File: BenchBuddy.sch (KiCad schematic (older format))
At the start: 0 parts

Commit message: Understanding the LED Driver Module
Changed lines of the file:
@@
 F0 "LED_Driver" 50
 F1 "LED_Driver.sch" 50
-F2 "EN" I L 6750 3250 60
-F3 "FREQ" I L 6750 3450 60
-F4 "String+" O R 8900 3250 60
-F5 "String-" I R 8900 3450 60
+F2 "String+" O R 8900 3250 60
+F3 "String-" I R 8900 3450 60
+F4 "LED_EN_PWM" I L 6750 3300 60
 $EndSheet
 $Sheet

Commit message: Understanding the Arduino Module
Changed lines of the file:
@@
 LIBS:valves
 LIBS:MyComponents
+LIBS:arduino_shieldsNCL
 LIBS:BenchBuddy-cache
 EELAYER 24 0
@@
 F2 "Relay+" O R 3450 6650 60
 F3 "Relay-" I R 3450 6850 60
-F4 "MOSI" O R 3450 5900 60
-F5 "MISO" I R 3450 6000 60
+F4 "MOSI" O R 3450 6050 60
+F5 "MISO" I R 3450 5950 60
 F6 "SCLK" O R 3450 6150 60
-F7 "CS_N" O R 3450 6300 60
-F8 "LED_EN" O R 3450 5300 60
-F9 "LED_FREQ" O R 3450 5450 60
-F10 "FAN_EN" O R 3450 4750 60
-F11 "FAN_MEAS" I R 3450 4950 60
+F7 "FAN_EN_N" O R 3450 5250 60
+F8 "CURR_MEAS" I R 3450 5450 60
+F9 "LED_EN_PWM" O R 3450 4750 60
+F10 "TACH_MEAS" I R 3450 5600 60
+F11 "V+_ADJ_MON" I R 3450 4000 60
+F12 "V-_ADJ_MON" I R 3450 4150 60
+F13 "DAC_CS_N" O R 3450 6250 60
+F14 "ADC_CS_N" O R 3450 6350 60
 $EndSheet
 $Sheet
@@
 F0 "Thermocouple" 50
 F1 "Thermocouple.sch" 50
-F2 "MOSI" I L 6750 4150 60
-F3 "MISO" O L 6750 4300 60
+F2 "MOSI" I L 6750 4350 60
+F3 "MISO" O L 6750 4250 60
 F4 "SCLK" I L 6750 4450 60
-F5 "CS_N" I L 6750 4600 60
+F5 "CS_N" I L 6750 4550 60
 F6 "TC_IN+" I R 8900 4200 60
 F7 "TC_IN-" I R 8900 4400 60
@@
 $EndSheet
 $Sheet
-S 6750 3050 2150 550
-U 52EA35F8
-F0 "LED_Driver" 50
-F1 "LED_Driver.sch" 50
-F2 "String+" O R 8900 3250 60
-F3 "String-" I R 8900 3450 60
-F4 "LED_EN_PWM" I L 6750 3300 60
-$EndSheet
-$Sheet
 S 9400 800  1450 5300
 U 52EA3891
 F0 "Terminal_Block" 50
 F1 "Terminal_Block.sch" 50
-$EndSheet
-$Sheet
-S 6750 1650 2150 1100
-U 52EA3640
-F0 "Fan" 50
-F1 "Fan.sch" 50
-F2 "Power+" O R 8900 1850 60
-F3 "Power-" I R 8900 2000 60
-F4 "Tach_In" I R 8900 2150 60
-F5 "Tach_Out" O L 6750 2600 60
-F6 "Fan_In" I L 6750 1750 60
-F7 "MISO" O L 6750 1950 60
-F8 "MOSI" I L 6750 2050 60
-F9 "SCLK" I L 6750 2150 60
-F10 "CS_N" I L 6750 2250 60
-F11 "Current_Measure" O L 6750 2450 60
+F2 "V+_ADJ" O L 9400 1150 60
+F3 "V-_ADJ" O L 9400 1350 60
+F4 "FAN_OUT+" O L 9400 2850 60
+F5 "FAN_OUT-" O L 9400 3000 60
+F6 "TACH_IN" I L 9400 3600 60
+F7 "LED_STRING+" O L 9400 2050 60
+F8 "LED_STRING-" O L 9400 2200 60
+F9 "RELAY_NC" B L 9400 5700 60
+F10 "RELAY_NO" B L 9400 5550 60
+F11 "RELAY_COM" B L 9400 5400 60
+F12 "TC_IN+" I L 9400 4200 60
+F13 "TC_IN-" I L 9400 4400 60
 $EndSheet
 $Sheet
@@
 F0 "Relay" 50
 F1 "Relay.sch" 50
-F2 "DIN+" I L 6750 5350 60
-F3 "DIN-" O L 6750 5700 60
-F4 "NC" B R 8900 5400 60
-F5 "NO" B R 8900 5700 60
-F6 "COM" B R 8900 5550 60
-$EndSheet
+F2 "RELAY_NC" B R 8900 5700 60
+F3 "RELAY_NO" B R 8900 5550 60
+F4 "RELAY_COM" B R 8900 5400 60
+F5 "RELAY+" I L 6750 5400 60
+F6 "RELAY-" O L 6750 5550 60
+$EndSheet
+$Sheet
+S 6750 1850 2150 550
+U 52EA35F8
+F0 "LED_Driver" 50
+F1 "LED_Driver.sch" 50
+F2 "LED_EN_PWM" I L 6750 2250 60
+F3 "LED_STRING+" O R 8900 2050 60
+F4 "LED_STRING-" O R 8900 2200 60
+$EndSheet
+Wire Wire Line
+	9400 1150 6300 1150
+Wire Wire Line
+	9400 1350 6300 1350
+Wire Wire Line
+	9400 5400 8900 5400
+Wire Wire Line
+	8900 5550 9400 5550
+Wire Wire Line
+	9400 5700 8900 5700
+Wire Wire Line
+	8900 4200 9400 4200
+Wire Wire Line
+	8900 4400 9400 4400
+Wire Wire Line
+	3450 4000 3800 4000
+Wire Wire Line
+	3800 4000 3800 1450
+Wire Wire Line
+	3800 1450 4150 1450
+Wire Wire Line
+	3450 4150 4000 4150
+Wire Wire Line
+	4000 4150 4000 1550
+Wire Wire Line
+	4000 1550 4150 1550
+$Sheet
+S 6750 2650 2150 1100
+U 52EA3640
+F0 "Fan" 50
+F1 "Fan.sch" 50
+F2 "MISO" O L 6750 3250 60
+F3 "MOSI" I L 6750 3350 60
+F4 "SCLK" I L 6750 3450 60
+F5 "CS_N" I L 6750 3550 60
+F6 "FAN_OUT+" O R 8900 2850 60
+F7 "TACH_IN" I R 8900 3600 60
+F8 "TACH_MEAS" O L 6750 3050 60
+F9 "FAN_EN_N" I L 6750 2800 60
+F10 "CURR_MEAS" O L 6750 2900 60
+F11 "FAN_OUT-" O R 8900 3000 60
+$EndSheet
+Wire Wire Line
+	9400 2050 8900 2050
+Wire Wire Line
+	8900 2200 9400 2200
+Wire Wire Line
+	9400 2850 8900 2850
+Wire Wire Line
+	8900 3000 9400 3000
+Wire Wire Line
+	9400 3600 8900 3600
+Wire Wire Line
+	6750 2250 4650 2250
+Wire Wire Line
+	4650 2250 4650 4750
+Wire Wire Line
+	4650 4750 3450 4750
+Wire Wire Line
+	3450 5250 5150 5250
+Wire Wire Line
+	5150 5250 5150 2800
+Wire Wire Line
+	5150 2800 6750 2800
+Wire Wire Line
+	3450 5450 5300 5450
+Wire Wire Line
+	5300 5450 5300 2900
+Wire Wire Line
+	5300 2900 6750 2900
+Wire Wire Line
+	3450 5600 5400 5600
+Wire Wire Line
+	5400 5600 5400 3050
+Wire Wire Line
+	5400 3050 6750 3050
+Wire Wire Line
+	3450 5950 5600 5950
+Wire Wire Line
+	5600 5950 5600 4250
+Wire Wire Line
+	5600 4250 5600 3250
+Wire Wire Line
+	5600 3250 6750 3250
+Wire Wire Line
+	6750 3350 5700 3350
+Wire Wire Line
+	5700 3350 5700 4350
+Wire Wire Line
+	5700 4350 5700 6050
+Wire Wire Line
+	5700 6050 3450 6050
+Wire Wire Line
+	3450 6150 5800 6150
+Wire Wire Line
+	5800 6150 5800 4450
+Wire Wire Line
+	5800 4450 5800 3450
+Wire Wire Line
+	5800 3450 6750 3450
+Wire Wire Line
+	6750 5400 6200 5400
+Wire Wire Line
+	6200 5400 6200 6650
+Wire Wire Line
+	6200 6650 3450 6650
+Wire Wire Line
+	3450 6850 6350 6850
+Wire Wire Line
+	6350 6850 6350 5550
+Wire Wire Line
+	6350 5550 6750 5550
+Wire Wire Line
+	3450 6250 5900 6250
+Wire Wire Line
+	5900 6250 5900 3550
+Wire Wire Line
+	5900 3550 6750 3550
+Wire Wire Line
+	6750 4250 5600 4250
+Connection ~ 5600 4250
+Wire Wire Line
+	6750 4350 5700 4350
+Connection ~ 5700 4350
+Wire Wire Line
+	6750 4450 5800 4450
+Connection ~ 5800 4450
+Wire Wire Line
+	6750 4550 6000 4550
+Wire Wire Line
+	6000 4550 6000 6350
+Wire Wire Line
+	6000 6350 3450 6350
 $EndSCHEMATC

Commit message: Revisting the Current/Fan Module
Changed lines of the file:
@@
 F5 "MISO" I R 3450 5950 60
 F6 "SCLK" O R 3450 6150 60
-F7 "FAN_EN_N" O R 3450 5250 60
-F8 "CURR_MEAS" I R 3450 5450 60
-F9 "LED_EN_PWM" O R 3450 4750 60
-F10 "TACH_MEAS" I R 3450 5600 60
-F11 "V+_ADJ_MON" I R 3450 4000 60
-F12 "V-_ADJ_MON" I R 3450 4150 60
-F13 "DAC_CS_N" O R 3450 6250 60
-F14 "ADC_CS_N" O R 3450 6350 60
+F7 "CURR_MEAS" I R 3450 5500 60
+F8 "LED_EN_PWM" O R 3450 4750 60
+F9 "TACH_MEAS" I R 3450 5600 60
+F10 "V+_ADJ_MON" I R 3450 4000 60
+F11 "V-_ADJ_MON" I R 3450 4150 60
+F12 "DAC_CS_N" O R 3450 6250 60
+F13 "ADC_CS_N" O R 3450 6350 60
+F14 "FAN_PWM" O R 3450 5250 60
+F15 "FAN_MODE" O R 3450 5350 60
 $EndSheet
 $Sheet
@@
 F0 "Fan" 50
 F1 "Fan.sch" 50
-F2 "MISO" O L 6750 3250 60
-F3 "MOSI" I L 6750 3350 60
-F4 "SCLK" I L 6750 3450 60
-F5 "CS_N" I L 6750 3550 60
+F2 "MISO" O L 6750 3350 60
+F3 "MOSI" I L 6750 3450 60
+F4 "SCLK" I L 6750 3550 60
+F5 "CS_N" I L 6750 3650 60
 F6 "FAN_OUT+" O R 8900 2850 60
 F7 "TACH_IN" I R 8900 3600 60
-F8 "TACH_MEAS" O L 6750 3050 60
-F9 "FAN_EN_N" I L 6750 2800 60
-F10 "CURR_MEAS" O L 6750 2900 60
-F11 "FAN_OUT-" O R 8900 3000 60
+F8 "TACH_MEAS" O L 6750 3150 60
+F9 "CURR_MEAS" O L 6750 3050 60
+F10 "FAN_OUT-" O R 8900 3000 60
+F11 "FAN_PWM" I L 6750 2800 60
+F12 "FAN_MODE" O L 6750 2900 60
 $EndSheet
 Wire Wire Line
@@
 	4650 4750 3450 4750
 Wire Wire Line
-	3450 5250 5150 5250
-Wire Wire Line
-	5150 5250 5150 2800
-Wire Wire Line
-	5150 2800 6750 2800
-Wire Wire Line
-	3450 5450 5300 5450
-Wire Wire Line
-	5300 5450 5300 2900
-Wire Wire Line
-	5300 2900 6750 2900
+	3450 5250 5100 5250
+Wire Wire Line
+	5100 5250 5100 2800
+Wire Wire Line
+	5100 2800 6750 2800
+Wire Wire Line
+	3450 5500 5300 5500
+Wire Wire Line
+	5300 5500 5300 3050
+Wire Wire Line
+	5300 3050 6750 3050
 Wire Wire Line
 	3450 5600 5400 5600
 Wire Wire Line
-	5400 5600 5400 3050
-Wire Wire Line
-	5400 3050 6750 3050
-Wire Wire Line
-	3450 5950 5600 5950
-Wire Wire Line
-	5600 5950 5600 4250
-Wire Wire Line
-	5600 4250 5600 3250
-Wire Wire Line
-	5600 3250 6750 3250
-Wire Wire Line
-	6750 3350 5700 3350
-Wire Wire Line
-	5700 3350 5700 4350
+	5400 5600 5400 3150
+Wire Wire Line
+	5400 3150 6750 3150
+Wire Wire Line
+	5600 5950 3450 5950
+Wire Wire Line
+	5600 3350 5600 4250
+Wire Wire Line
+	5600 4250 5600 5950
+Wire Wire Line
+	5600 3350 6750 3350
+Wire Wire Line
+	6750 3450 5700 3450
+Wire Wire Line
+	5700 3450 5700 4350
 Wire Wire Line
 	5700 4350 5700 6050
@@
 	5700 6050 3450 6050
 Wire Wire Line
-	3450 6150 5800 6150
-Wire Wire Line
-	5800 6150 5800 4450
-Wire Wire Line
-	5800 4450 5800 3450
-Wire Wire Line
-	5800 3450 6750 3450
+	5800 6150 3450 6150
+Wire Wire Line
+	5800 3550 5800 4450
+Wire Wire Line
+	5800 4450 5800 6150
+Wire Wire Line
+	5800 3550 6750 3550
 Wire Wire Line
 	6750 5400 6200 5400
@@
 	3450 6250 5900 6250
 Wire Wire Line
-	5900 6250 5900 3550
-Wire Wire Line
-	5900 3550 6750 3550
+	5900 6250 5900 3650
+Wire Wire Line
+	5900 3650 6750 3650
 Wire Wire Line
 	6750 4250 5600 4250
@@
 Wire Wire Line
 	6000 6350 3450 6350
+Wire Wire Line
+	6750 2900 5200 2900
+Wire Wire Line
+	5200 5350 5200 2900
+Wire Wire Line
+	3450 5350 5200 5350
 $EndSCHEMATC

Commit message: Associating and Placing the Relay Module
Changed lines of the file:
@@
 	5600 5950 3450 5950
 Wire Wire Line
-	5600 3350 5600 4250
-Wire Wire Line
-	5600 4250 5600 5950
+	5600 3350 5600 5950
 Wire Wire Line
 	5600 3350 6750 3350
@@
 	6750 3450 5700 3450
 Wire Wire Line
-	5700 3450 5700 4350
-Wire Wire Line
-	5700 4350 5700 6050
+	5700 3450 5700 6050
 Wire Wire Line
 	5700 6050 3450 6050
@@
 	5800 6150 3450 6150
 Wire Wire Line
-	5800 3550 5800 4450
-Wire Wire Line
-	5800 4450 5800 6150
+	5800 3550 5800 6150
 Wire Wire Line
 	5800 3550 6750 3550
@@
 	6750 2900 5200 2900
 Wire Wire Line
-	5200 5350 5200 2900
+	5200 2900 5200 5350
 Wire Wire Line
-	3450 5350 5200 5350
+	5200 5350 3450 5350
 $EndSCHEMATC

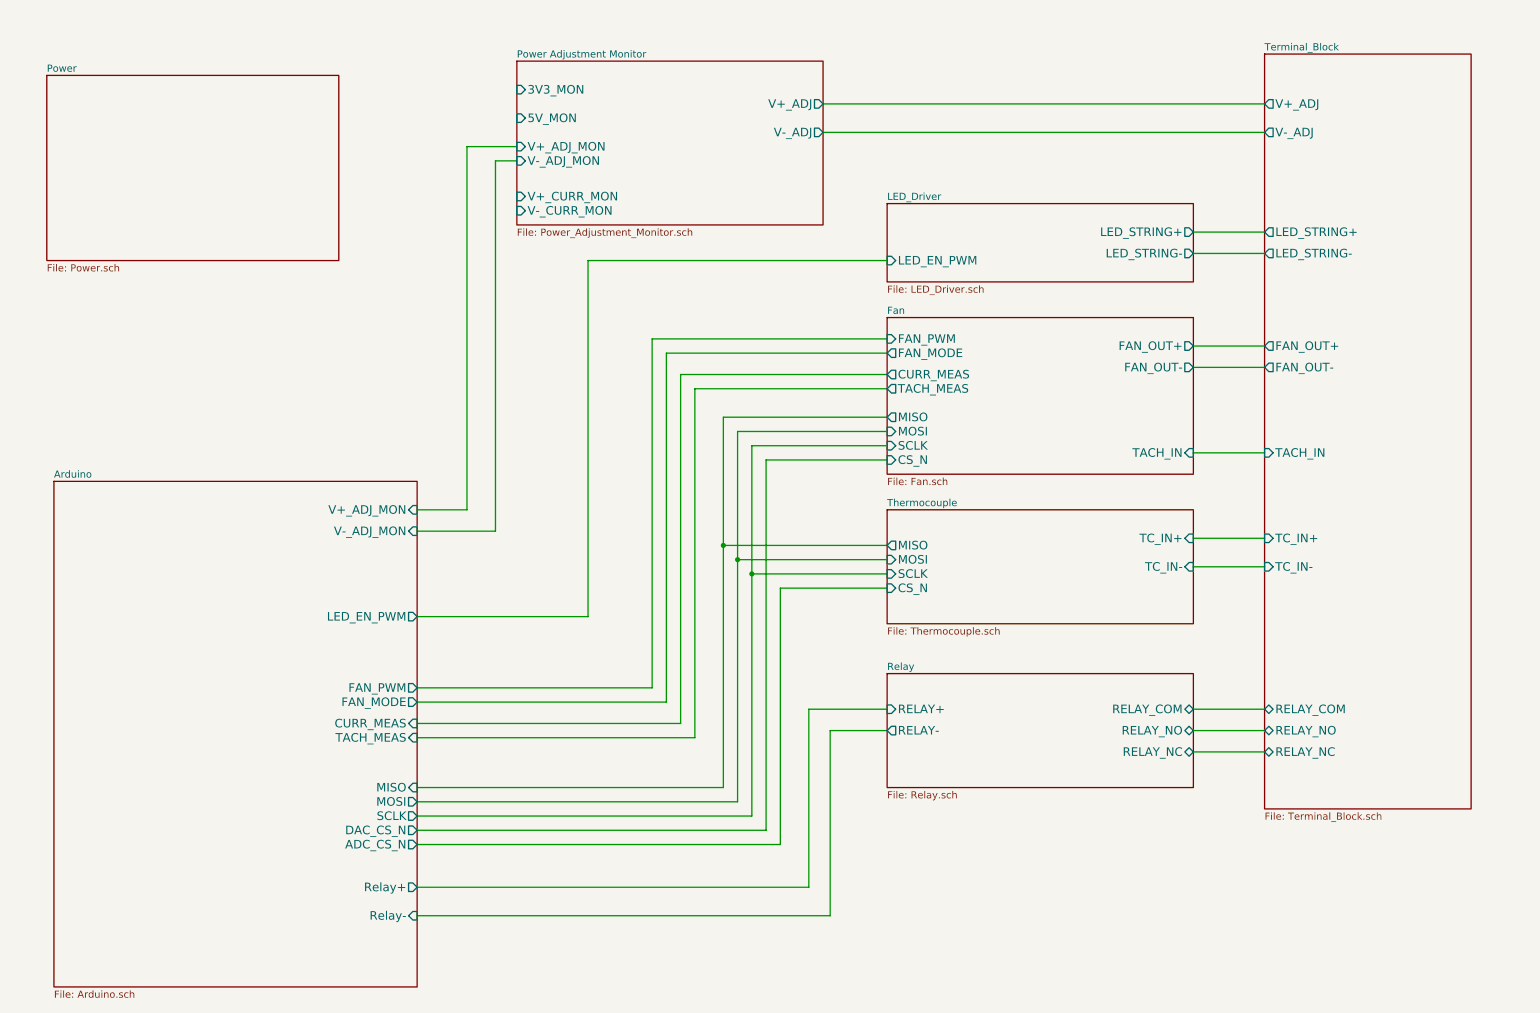
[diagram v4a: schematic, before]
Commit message: Associating and Placing the Thermocouple Module
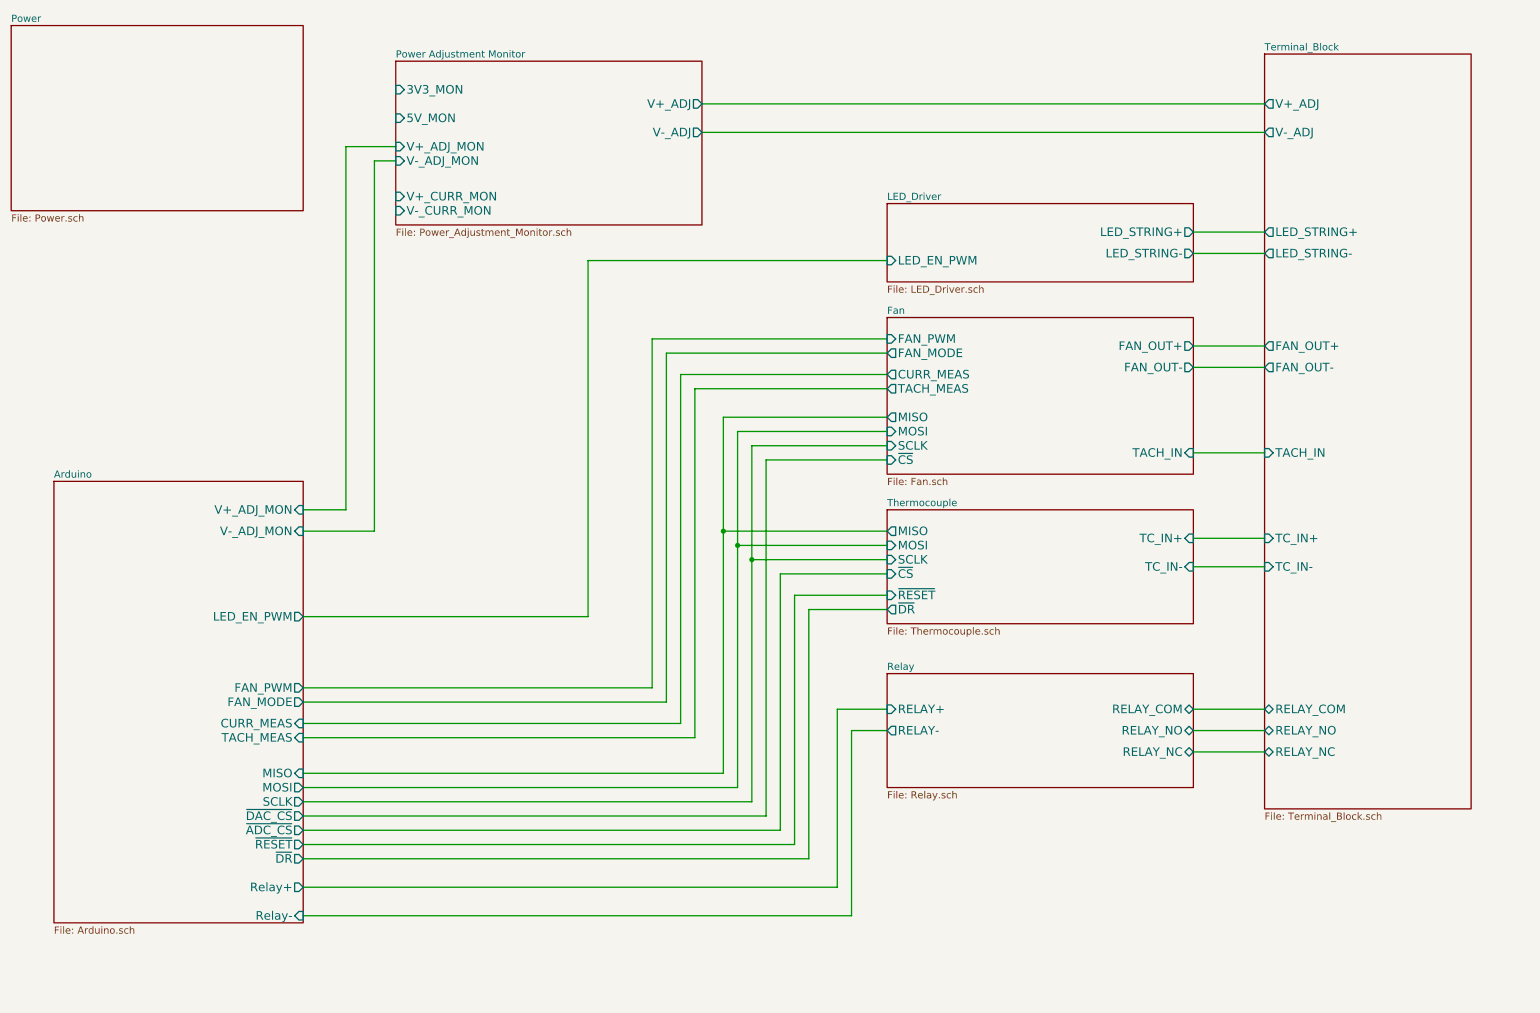
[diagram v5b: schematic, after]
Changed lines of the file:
@@
 LIBS:MyComponents
 LIBS:arduino_shieldsNCL
+LIBS:BenchBudEE
 LIBS:BenchBuddy-cache
 EELAYER 24 0
@@
 $EndDescr
 $Sheet
-S 900  3800 2550 3550
+S 900  3800 1750 3100
 U 52EA34C7
 F0 "Arduino" 50
 F1 "Arduino.sch" 50
-F2 "Relay+" O R 3450 6650 60
-F3 "Relay-" I R 3450 6850 60
-F4 "MOSI" O R 3450 6050 60
-F5 "MISO" I R 3450 5950 60
-F6 "SCLK" O R 3450 6150 60
-F7 "CURR_MEAS" I R 3450 5500 60
-F8 "LED_EN_PWM" O R 3450 4750 60
-F9 "TACH_MEAS" I R 3450 5600 60
-F10 "V+_ADJ_MON" I R 3450 4000 60
-F11 "V-_ADJ_MON" I R 3450 4150 60
-F12 "DAC_CS_N" O R 3450 6250 60
-F13 "ADC_CS_N" O R 3450 6350 60
-F14 "FAN_PWM" O R 3450 5250 60
-F15 "FAN_MODE" O R 3450 5350 60
+F2 "Relay+" O R 2650 6650 60
+F3 "Relay-" I R 2650 6850 60
+F4 "MOSI" O R 2650 5950 60
+F5 "MISO" I R 2650 5850 60
+F6 "SCLK" O R 2650 6050 60
+F7 "CURR_MEAS" I R 2650 5500 60
+F8 "LED_EN_PWM" O R 2650 4750 60
+F9 "TACH_MEAS" I R 2650 5600 60
+F10 "V+_ADJ_MON" I R 2650 4000 60
+F11 "V-_ADJ_MON" I R 2650 4150 60
+F12 "FAN_PWM" O R 2650 5250 60
+F13 "FAN_MODE" O R 2650 5350 60
+F14 "~DAC_CS" O R 2650 6150 60
+F15 "~ADC_CS" O R 2650 6250 60
+F16 "~RESET" O R 2650 6350 60
+F17 "~DR" O R 2650 6450 60
 $EndSheet
 $Sheet
@@
 F0 "Thermocouple" 50
 F1 "Thermocouple.sch" 50
-F2 "MOSI" I L 6750 4350 60
-F3 "MISO" O L 6750 4250 60
-F4 "SCLK" I L 6750 4450 60
-F5 "CS_N" I L 6750 4550 60
-F6 "TC_IN+" I R 8900 4200 60
-F7 "TC_IN-" I R 8900 4400 60
-$EndSheet
-$Sheet
-S 850  950  2050 1300
+F2 "MOSI" I L 6750 4250 60
+F3 "MISO" O L 6750 4150 60
+F4 "SCLK" I L 6750 4350 60
+F5 "TC_IN+" I R 8900 4200 60
+F6 "TC_IN-" I R 8900 4400 60
+F7 "~CS" I L 6750 4450 60
+F8 "~RESET" I L 6750 4600 60
+F9 "~DR" O L 6750 4700 60
+$EndSheet
+$Sheet
+S 600  600  2050 1300
 U 52EA35B5
 F0 "Power" 50
@@
 $EndSheet
 $Sheet
-S 4150 850  2150 1150
+S 3300 850  2150 1150
 U 52F220BB
 F0 "Power Adjustment Monitor" 50
 F1 "Power_Adjustment_Monitor.sch" 50
-F2 "V+_ADJ" O R 6300 1150 60
-F3 "V-_ADJ" O R 6300 1350 60
-F4 "3V3_MON" I L 4150 1050 60
-F5 "5V_MON" I L 4150 1250 60
-F6 "V+_ADJ_MON" I L 4150 1450 60
-F7 "V-_ADJ_MON" I L 4150 1550 60
-F8 "V+_CURR_MON" I L 4150 1800 60
-F9 "V-_CURR_MON" I L 4150 1900 60
+F2 "V+_ADJ" O R 5450 1150 60
+F3 "V-_ADJ" O R 5450 1350 60
+F4 "3V3_MON" I L 3300 1050 60
+F5 "5V_MON" I L 3300 1250 60
+F6 "V+_ADJ_MON" I L 3300 1450 60
+F7 "V-_ADJ_MON" I L 3300 1550 60
+F8 "V+_CURR_MON" I L 3300 1800 60
+F9 "V-_CURR_MON" I L 3300 1900 60
 $EndSheet
 $Sheet
@@
 $EndSheet
 Wire Wire Line
-	9400 1150 6300 1150
-Wire Wire Line
-	9400 1350 6300 1350
+	9400 1150 5450 1150
+Wire Wire Line
+	9400 1350 5450 1350
 Wire Wire Line
 	9400 5400 8900 5400
@@
 	8900 4400 9400 4400
 Wire Wire Line
-	3450 4000 3800 4000
-Wire Wire Line
-	3800 4000 3800 1450
-Wire Wire Line
-	3800 1450 4150 1450
-Wire Wire Line
-	3450 4150 4000 4150
-Wire Wire Line
-	4000 4150 4000 1550
-Wire Wire Line
-	4000 1550 4150 1550
+	2950 1450 3300 1450
+Wire Wire Line
+	3150 1550 3300 1550
 $Sheet
 S 6750 2650 2150 1100
@@
 F3 "MOSI" I L 6750 3450 60
 F4 "SCLK" I L 6750 3550 60
-F5 "CS_N" I L 6750 3650 60
-F6 "FAN_OUT+" O R 8900 2850 60
-F7 "TACH_IN" I R 8900 3600 60
-F8 "TACH_MEAS" O L 6750 3150 60
-F9 "CURR_MEAS" O L 6750 3050 60
-F10 "FAN_OUT-" O R 8900 3000 60
-F11 "FAN_PWM" I L 6750 2800 60
-F12 "FAN_MODE" O L 6750 2900 60
+F5 "FAN_OUT+" O R 8900 2850 60
+F6 "TACH_IN" I R 8900 3600 60
+F7 "TACH_MEAS" O L 6750 3150 60
+F8 "CURR_MEAS" O L 6750 3050 60
+F9 "FAN_OUT-" O R 8900 3000 60
+F10 "FAN_PWM" I L 6750 2800 60
+F11 "FAN_MODE" O L 6750 2900 60
+F12 "~CS" I L 6750 3650 60
 $EndSheet
 Wire Wire Line
@@
 	4650 2250 4650 4750
 Wire Wire Line
-	4650 4750 3450 4750
-Wire Wire Line
-	3450 5250 5100 5250
+	4650 4750 2650 4750
+Wire Wire Line
+	2650 5250 5100 5250
 Wire Wire Line
 	5100 5250 5100 2800
@@
 	5100 2800 6750 2800
 Wire Wire Line
-	3450 5500 5300 5500
+	2650 5500 5300 5500
 Wire Wire Line
 	5300 5500 5300 3050
@@
 	5300 3050 6750 3050
 Wire Wire Line
-	3450 5600 5400 5600
+	2650 5600 5400 5600
 Wire Wire Line
 	5400 5600 5400 3150
@@
 	5400 3150 6750 3150
 Wire Wire Line
-	5600 5950 3450 5950
-Wire Wire Line
-	5600 3350 5600 5950
+	5600 5850 2650 5850
+Wire Wire Line
+	5600 3350 5600 5850
 Wire Wire Line
 	5600 3350 6750 3350
@@
 	6750 3450 5700 3450
 Wire Wire Line
-	5700 3450 5700 6050
-Wire Wire Line
-	5700 6050 3450 6050
-Wire Wire Line
-	5800 6150 3450 6150
-Wire Wire Line
-	5800 3550 5800 6150
+	5700 3450 5700 5950
+Wire Wire Line
+	5700 5950 2650 5950
+Wire Wire Line
+	5800 6050 2650 6050
+Wire Wire Line
+	5800 3550 5800 6050
 Wire Wire Line
 	5800 3550 6750 3550
 Wire Wire Line
-	6750 5400 6200 5400
-Wire Wire Line
-	6200 5400 6200 6650
-Wire Wire Line
-	6200 6650 3450 6650
-Wire Wire Line
-	3450 6850 6350 6850
-Wire Wire Line
-	6350 6850 6350 5550
-Wire Wire Line
-	6350 5550 6750 5550
-Wire Wire Line
-	3450 6250 5900 6250
-Wire Wire Line
-	5900 6250 5900 3650
+	6750 5400 6400 5400
+Wire Wire Line
+	6400 5400 6400 6650
+Wire Wire Line
+	6400 6650 2650 6650
+Wire Wire Line
+	2650 6850 6500 6850
+Wire Wire Line
+	6500 6850 6500 5550
+Wire Wire Line
+	6500 5550 6750 5550
+Wire Wire Line
+	2650 6150 5900 6150
+Wire Wire Line
+	5900 6150 5900 3650
 Wire Wire Line
 	5900 3650 6750 3650
 Wire Wire Line
-	6750 4250 5600 4250
-Connection ~ 5600 4250
-Wire Wire Line
-	6750 4350 5700 4350
-Connection ~ 5700 4350
-Wire Wire Line
-	6750 4450 5800 4450
-Connection ~ 5800 4450
-Wire Wire Line
-	6750 4550 6000 4550
-Wire Wire Line
-	6000 4550 6000 6350
-Wire Wire Line
-	6000 6350 3450 6350
+	6750 4150 5600 4150
+Connection ~ 5600 4150
+Wire Wire Line
+	6750 4250 5700 4250
+Connection ~ 5700 4250
+Wire Wire Line
+	6750 4350 5800 4350
+Connection ~ 5800 4350
+Wire Wire Line
+	6750 4450 6000 4450
+Wire Wire Line
+	6000 4450 6000 6250
+Wire Wire Line
+	6000 6250 2650 6250
 Wire Wire Line
 	6750 2900 5200 2900
@@
 	5200 2900 5200 5350
 Wire Wire Line
-	5200 5350 3450 5350
+	5200 5350 2650 5350
+Wire Wire Line
+	2950 1450 2950 4000
+Wire Wire Line
+	2950 4000 2650 4000
+Wire Wire Line
+	3150 1550 3150 4150
+Wire Wire Line
+	3150 4150 2650 4150
+Wire Wire Line
+	6750 4600 6100 4600
+Wire Wire Line
+	6100 4600 6100 6350
+Wire Wire Line
+	6100 6350 2650 6350
+Wire Wire Line
+	6750 4700 6200 4700
+Wire Wire Line
+	6200 4700 6200 6450
+Wire Wire Line
+	6200 6450 2650 6450
 $EndSCHEMATC
